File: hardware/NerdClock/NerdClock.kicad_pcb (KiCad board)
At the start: 2 copper layers, 95 x 95 mm, 0 parts

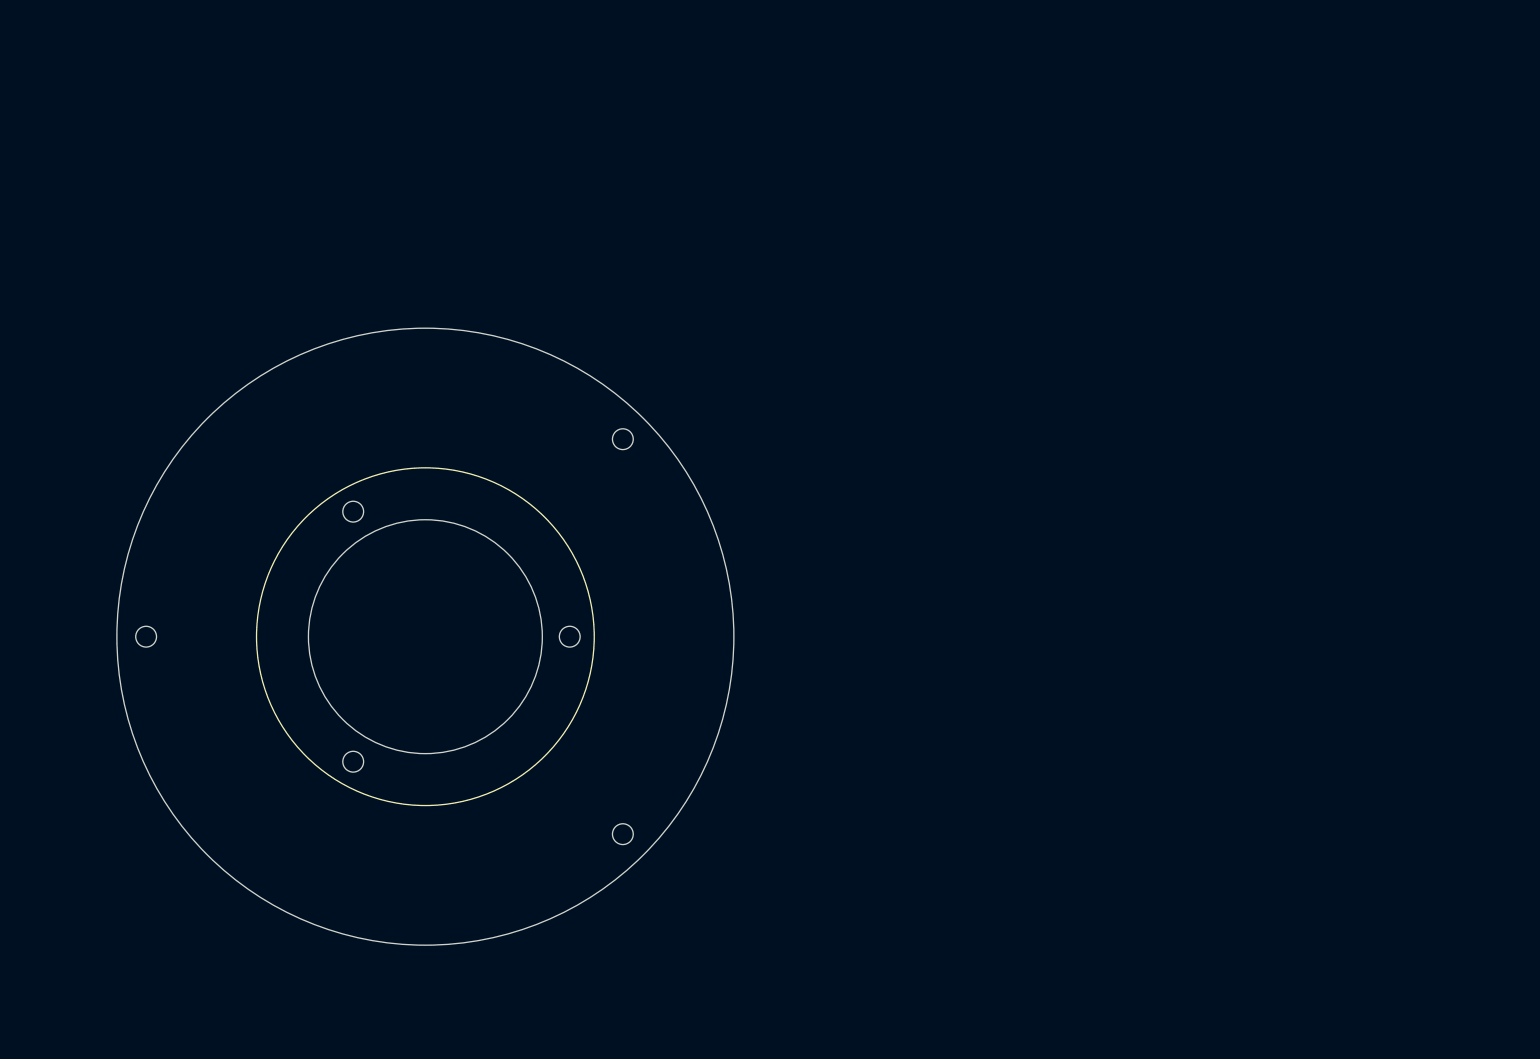
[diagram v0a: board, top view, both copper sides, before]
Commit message: Added breakout tabs
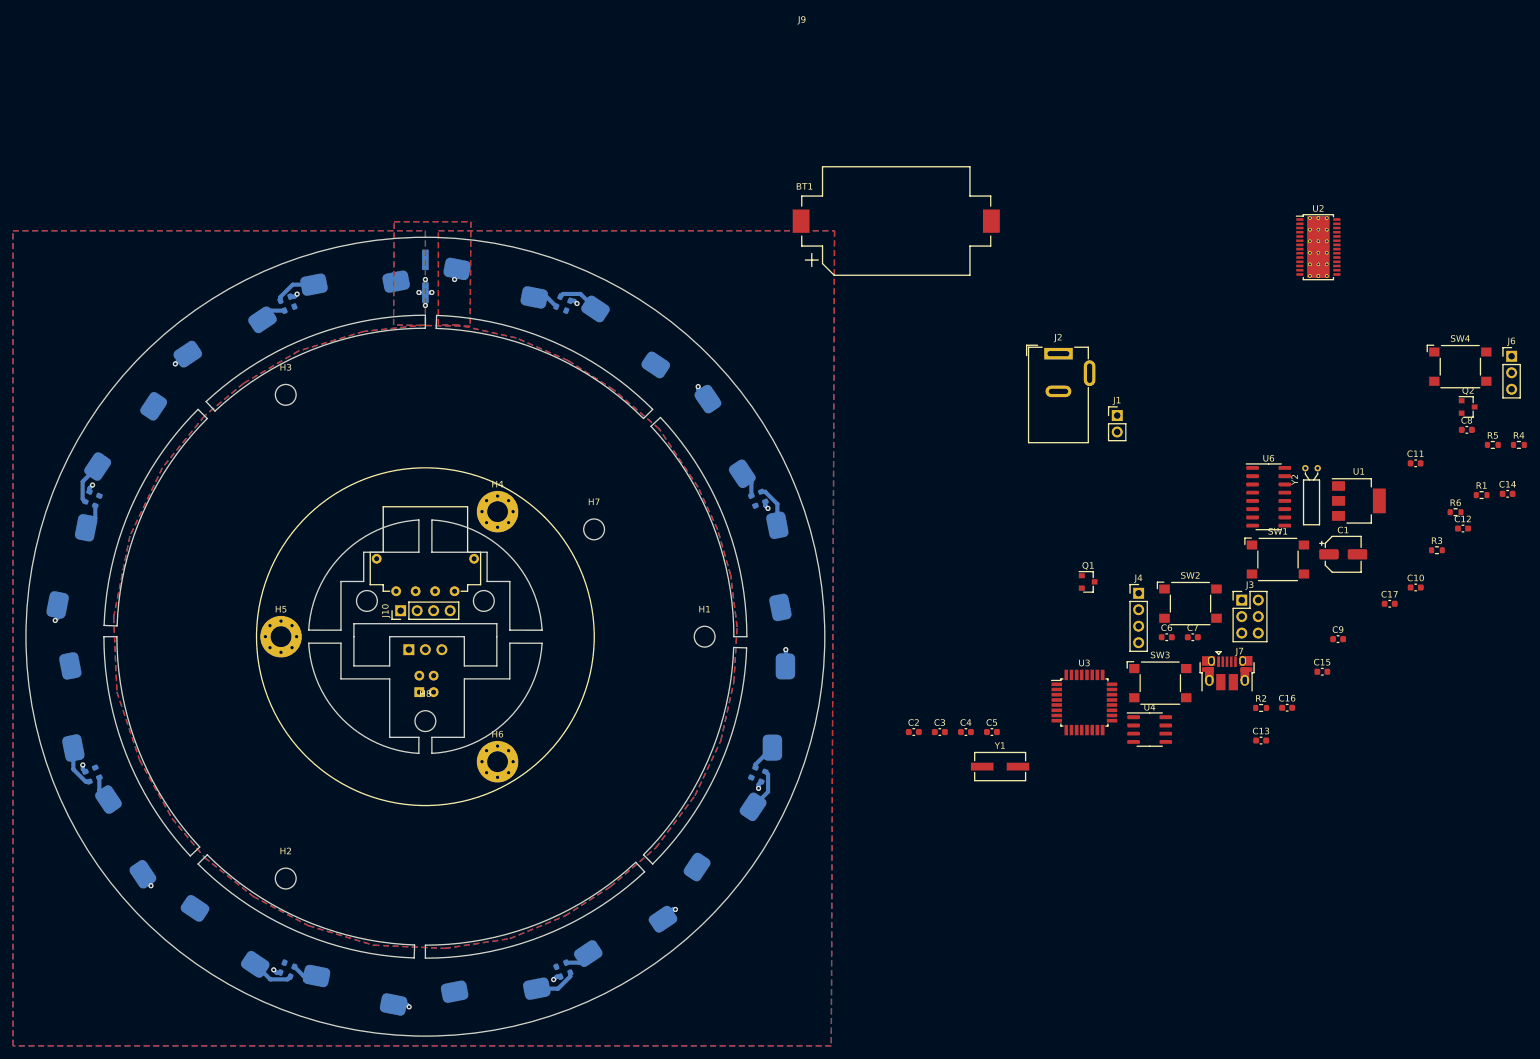
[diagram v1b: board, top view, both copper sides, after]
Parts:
- added BT1: Battery_Cell, Battery:BatteryHolder_Keystone_1060_1x2032, F.Cu at (172.5, 36.0)
- added C1: 100u, Capacitor_SMD:CP_Elec_5x5.4, F.Cu at (241.3, 87.3)
- added C10: 100n, Capacitor_SMD:C_0603_1608Metric, F.Cu at (252.5, 92.4)
- added C11: 100n, Capacitor_SMD:C_0603_1608Metric, F.Cu at (252.5, 73.3)
- added C12: 18p, Capacitor_SMD:C_0603_1608Metric, F.Cu at (259.8, 83.3)
- added C13: 0.47u, Capacitor_SMD:C_0603_1608Metric, F.Cu at (228.7, 116.0)
- added C14: 18p, Capacitor_SMD:C_0603_1608Metric, F.Cu at (266.6, 78.0)
- added C15: 100n, Capacitor_SMD:C_0603_1608Metric, F.Cu at (238.1, 105.4)
- added C16: 100n, Capacitor_SMD:C_0603_1608Metric, F.Cu at (232.7, 110.9)
- added C17: 100n, Capacitor_SMD:C_0603_1608Metric, F.Cu at (248.5, 94.9)
- added C2: 100n, Capacitor_SMD:C_0603_1608Metric, F.Cu at (175.2, 114.7)
- added C3: 10u, Capacitor_SMD:C_0603_1608Metric, F.Cu at (179.2, 114.7)
- added C4: 10n, Capacitor_SMD:C_0603_1608Metric, F.Cu at (183.2, 114.7)
- added C5: 100n, Capacitor_SMD:C_0603_1608Metric, F.Cu at (187.2, 114.7)
- added C6: 100n, Capacitor_SMD:C_0603_1608Metric, F.Cu at (214.2, 100.1)
- added C7: 100n, Capacitor_SMD:C_0603_1608Metric, F.Cu at (218.2, 100.1)
- added C8: 100n, Capacitor_SMD:C_0603_1608Metric, F.Cu at (260.4, 68.2)
- added C9: 100n, Capacitor_SMD:C_0603_1608Metric, F.Cu at (240.5, 100.4)
- added D1: LED, WhiteLed1W:WhiteLed1W, B.Cu at (110.8, 45.6)
- added D10: LED, WhiteLed1W:WhiteLed1W, B.Cu at (69.2, 146.1)
- added D11: LED, WhiteLed1W:WhiteLed1W, B.Cu at (53.9, 130.8)
- added D12: LED, WhiteLed1W:WhiteLed1W, B.Cu at (45.6, 110.8)
- added D13: LED, WhiteLed1W:WhiteLed1W, B.Cu at (45.6, 89.2)
- added D14: LED, WhiteLed1W:WhiteLed1W, B.Cu at (53.9, 69.2)
- added D15: LED, WhiteLed1W:WhiteLed1W, B.Cu at (69.2, 53.9)
- added D16: LED, WhiteLed1W:WhiteLed1W, B.Cu at (89.2, 45.6)
- added D2: LED, WhiteLed1W:WhiteLed1W, B.Cu at (130.8, 53.9)
- added D3: LED, WhiteLed1W:WhiteLed1W, B.Cu at (146.1, 69.2)
- added D4: LED, WhiteLed1W:WhiteLed1W, B.Cu at (154.4, 89.2)
- added D5: LED, WhiteLed1W:WhiteLed1W, B.Cu at (154.4, 110.8)
- added D6: LED, WhiteLed1W:WhiteLed1W, B.Cu at (146.1, 130.8)
- added D7: LED, WhiteLed1W:WhiteLed1W, B.Cu at (130.8, 146.1)
- added D8: LED, WhiteLed1W:WhiteLed1W, B.Cu at (110.8, 154.4)
- added D9: LED, WhiteLed1W:WhiteLed1W, B.Cu at (89.2, 154.4)
- added H1: MountingHole, MountingHole:MountingHole_3.2mm_M3, F.Cu at (143.0, 100.0)
- added H10: MountingHole, MountingHole:MountingHole_3.2mm_M3, F.Cu at (109.0, 94.5)
- added H2: MountingHole, MountingHole:MountingHole_3.2mm_M3, F.Cu at (78.5, 137.2)
- added H3: MountingHole, MountingHole:MountingHole_3.2mm_M3, F.Cu at (78.5, 62.8)
- added H4: MountingHole_Pad, MountingHole:MountingHole_3.2mm_M3_Pad_Via, F.Cu at (111.1, 80.7)
- added H5: MountingHole_Pad, MountingHole:MountingHole_3.2mm_M3_Pad_Via, F.Cu at (77.8, 100.0)
- added H6: MountingHole_Pad, MountingHole:MountingHole_3.2mm_M3_Pad_Via, F.Cu at (111.1, 119.3)
- added H7: MountingHole, MountingHole:MountingHole_3.2mm_M3, F.Cu at (126.0, 83.5)
- added H8: MountingHole, MountingHole:MountingHole_3.2mm_M3, F.Cu at (100.0, 113.0)
- added H9: MountingHole, MountingHole:MountingHole_3.2mm_M3, F.Cu at (91.0, 94.5)
- added J1: Conn_01x02, Connector_PinHeader_2.54mm:PinHeader_1x02_P2.54mm_Vertical, F.Cu at (206.5, 65.9)
- added J10: Conn_01x04, Connector_PinHeader_2.54mm:PinHeader_1x04_P2.54mm_Vertical, F.Cu at (96.2, 96.0)
- added J2: Jack-DC, Connector_BarrelJack:BarrelJack_Wuerth_6941xx301002, F.Cu at (197.5, 56.4)
- added J3: ICSP, Connector_PinHeader_2.54mm:PinHeader_2x03_P2.54mm_Vertical, F.Cu at (225.7, 94.4)
- added J4: Conn_01x04, Connector_PinHeader_2.54mm:PinHeader_1x04_P2.54mm_Vertical, F.Cu at (209.8, 93.3)
- added J5: Conn_01x03, Connector_PinHeader_2.54mm:PinHeader_1x03_P2.54mm_Vertical, B.Cu at (97.5, 102.0)
- added J6: Conn_01x03, Connector_PinHeader_2.54mm:PinHeader_1x03_P2.54mm_Vertical, F.Cu at (267.3, 56.8)
- added J7: USB_B_Micro, Connector_USB:USB_Micro-B_Amphenol_10103594-0001LF_Horizontal, F.Cu at (223.5, 105.6)
- added J8: Conn_01x02, Connector_PinHeader_2.54mm:PinHeader_2x01_P2.54mm_Vertical_SMD, B.Cu at (100.0, 44.5)
- added J9: Conn_01x05, MotorConn:MotorConn, F.Cu at (100.0, 93.0)
- added Q1: RTR025N03FRATL, Package_TO_SOT_SMD:SOT-23, F.Cu at (202.1, 91.6)
- added Q2: RTR025N03FRATL, Package_TO_SOT_SMD:SOT-23, F.Cu at (260.6, 64.6)
- added R1: 300R, Resistor_SMD:R_0603_1608Metric, F.Cu at (262.6, 78.2)
- added R10: 22R, Resistor_SMD:R_0603_1608Metric, B.Cu at (152.0, 78.4)
- added R11: 22R, Resistor_SMD:R_0603_1608Metric, B.Cu at (150.5, 120.9)
- added R12: 22R, Resistor_SMD:R_0603_1608Metric, B.Cu at (152.0, 121.6)
- added R13: 22R, Resistor_SMD:R_0603_1608Metric, B.Cu at (120.9, 150.5)
- added R14: 22R, Resistor_SMD:R_0603_1608Metric, B.Cu at (121.6, 152.0)
- added R15: 22R, Resistor_SMD:R_0603_1608Metric, B.Cu at (79.1, 150.5)
- added R16: 22R, Resistor_SMD:R_0603_1608Metric, B.Cu at (78.4, 152.0)
- added R17: 22R, Resistor_SMD:R_0603_1608Metric, B.Cu at (49.5, 120.9)
- added R18: 22R, Resistor_SMD:R_0603_1608Metric, B.Cu at (48.0, 121.6)
- added R19: 22R, Resistor_SMD:R_0603_1608Metric, B.Cu at (49.5, 79.1)
- added R2: 300R, Resistor_SMD:R_0603_1608Metric, F.Cu at (228.7, 111.0)
- added R20: 22R, Resistor_SMD:R_0603_1608Metric, B.Cu at (48.0, 78.4)
- added R21: 22R, Resistor_SMD:R_0603_1608Metric, B.Cu at (79.1, 49.5)
- added R22: 22R, Resistor_SMD:R_0603_1608Metric, B.Cu at (78.4, 48.0)
- added R3: 20k, Resistor_SMD:R_0603_1608Metric, F.Cu at (255.8, 86.7)
- added R4: 10k, Resistor_SMD:R_0603_1608Metric, F.Cu at (268.4, 70.5)
- added R5: 4k7, Resistor_SMD:R_0603_1608Metric, F.Cu at (264.4, 70.5)
- added R6: 4k7, Resistor_SMD:R_0603_1608Metric, F.Cu at (258.6, 80.8)
- added R7: 22R, Resistor_SMD:R_0603_1608Metric, B.Cu at (120.9, 49.5)
- added R8: 22R, Resistor_SMD:R_0603_1608Metric, B.Cu at (121.6, 48.0)
- added R9: 22R, Resistor_SMD:R_0603_1608Metric, B.Cu at (150.5, 79.1)
- added SW1: SW_MEC_5G, Button_Switch_SMD:SW_SPST_Omron_B3FS-100xP, F.Cu at (231.3, 88.1)
- added SW2: SW_MEC_5G, Button_Switch_SMD:SW_SPST_Omron_B3FS-100xP, F.Cu at (217.8, 94.9)
- added SW3: SW_MEC_5G, Button_Switch_SMD:SW_SPST_Omron_B3FS-100xP, F.Cu at (213.2, 107.2)
- added SW4: SW_MEC_5G, Button_Switch_SMD:SW_SPST_Omron_B3FS-100xP, F.Cu at (259.4, 58.4)
- added U1: IFX1117, Package_TO_SOT_SMD:SOT-223-3_TabPin2, F.Cu at (243.7, 79.1)
- added U2: DRV8313, Package_SO:HTSSOP-28-1EP_4.4x9.7mm_P0.65mm_EP3.4x9.5mm_ThermalVias, F.Cu at (237.5, 40.0)
- added U3: ATmega168P-20AU, Package_QFP:TQFP-32_7x7mm_P0.8mm, F.Cu at (201.5, 110.1)
- added U4: DS1338Z-18+, Package_SO:SOIC-8_3.9x4.9mm_P1.27mm, F.Cu at (211.5, 114.3)
- added U5: OPB706A, OPB706A:OPB706A, B.Cu at (100.2, 107.3)
- added U6: CH340C, Package_SO:SOIC-16_3.9x9.9mm_P1.27mm, F.Cu at (229.8, 78.5)
- added Y1: 16MHz, Crystal:Crystal_SMD_ECS_CSM3X-2Pin_7.6x4.1mm, F.Cu at (188.5, 120.0)
- added Y2: 32.768kHz/12.5pf, Crystal:Crystal_C26-LF_D2.1mm_L6.5mm_Horizontal, F.Cu at (235.5, 74.1)
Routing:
- net Net-(D1-Pad1): track 0.00 -> 35.1 mm, vias 0 -> 20
- net Net-(D16-Pad1): track 0.00 -> 6.54 mm
- net Net-(D12-Pad1): track 0.00 -> 6.54 mm
- net Net-(D8-Pad1): track 0.00 -> 6.54 mm
- net Net-(D4-Pad1): track 0.00 -> 6.54 mm
- net Net-(D2-Pad1): track 0.00 -> 6.54 mm
- net Net-(D14-Pad1): track 0.00 -> 6.54 mm
- net Net-(D6-Pad1): track 0.00 -> 6.54 mm
- net Net-(D10-Pad1): track 0.00 -> 6.54 mm
- net Net-(D5-Pad2): track 0.00 -> 4.16 mm
- net Net-(D15-Pad2): track 0.00 -> 3.98 mm
- net Net-(D11-Pad2): track 0.00 -> 3.98 mm
- net Net-(D7-Pad2): track 0.00 -> 3.98 mm
- net Net-(D3-Pad2): track 0.00 -> 3.98 mm
- net Net-(D9-Pad2): track 0.00 -> 3.98 mm
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- added copper zone on F.Cu, net Net-(D1-Pad1)
- added copper zone on B.Cu, net Net-(D10-Pad2)
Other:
- board size 95 x 95 mm -> 123 x 123 mm

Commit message: Put LEDs on the right side (wtffff)
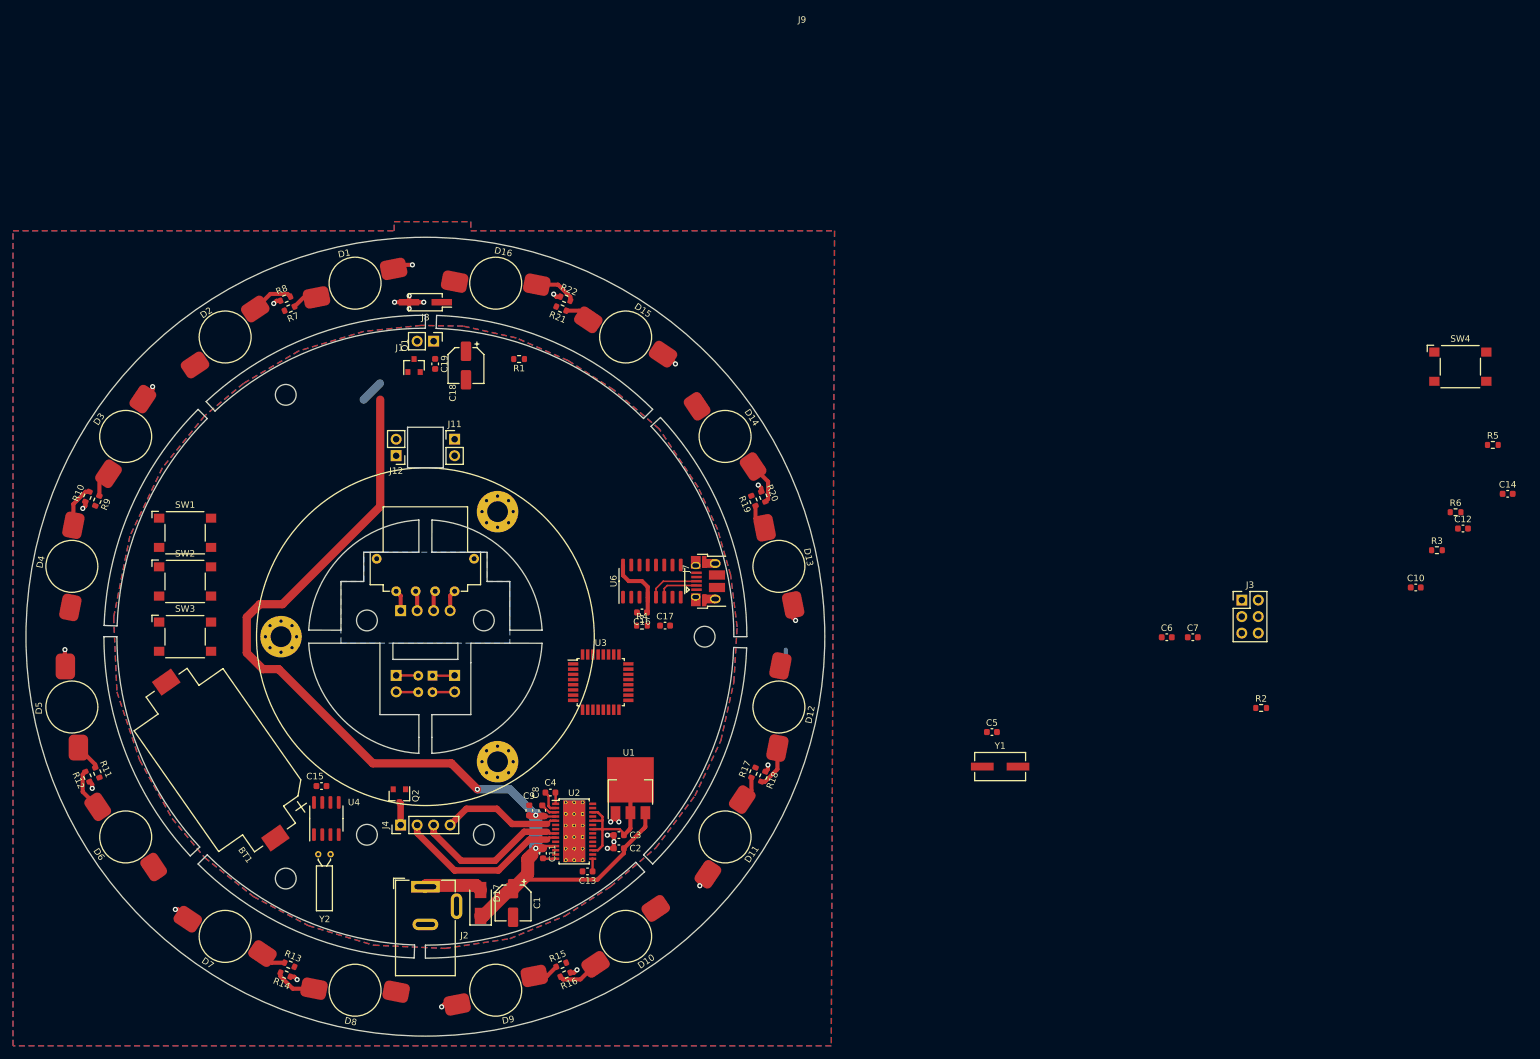
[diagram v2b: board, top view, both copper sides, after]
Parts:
- removed H7, H8: MountingHole, MountingHole:MountingHole_3.2mm_M3
- added C18: 100u, Capacitor_SMD:CP_Elec_5x5.4, F.Cu at (106.2, 58.2)
- added C19: 100n, Capacitor_SMD:C_0603_1608Metric, F.Cu at (101.5, 58.0)
- added D17: S1JL R3, Diode_SMD:D_SMA, F.Cu at (108.5, 141.0)
- added H11: MountingHole, MountingHole:MountingHole_3.2mm_M3, F.Cu at (109.0, 130.5)
- added H12: MountingHole, MountingHole:MountingHole_3.2mm_M3, F.Cu at (91.0, 130.5)
- added J11: Conn_01x02, Connector_PinHeader_2.54mm:PinHeader_1x02_P2.54mm_Vertical, F.Cu at (104.5, 69.6)
- added J12: Conn_01x02, Connector_PinHeader_2.54mm:PinHeader_1x02_P2.54mm_Vertical, F.Cu at (95.5, 72.1)
- D1, D10, D11, D12, D13, D14, D15, D16, D2, D3, D4, D5, D6, D7, D8, D9, J8, R10, R11, R12, R13, R14, R15, R16, R17, R18, R19, R20, R21, R22, R7, R8, R9: moved to F.Cu
- J10: moved to B.Cu
- J5: value Conn_01x03 -> Conn_01x02; footprint Connector_PinHeader_2.54mm:PinHeader_1x03_P2.54mm_Vertical -> Connector_PinHeader_2.54mm:PinHeader_1x02_P2.54mm_Vertical
- J6: value Conn_01x03 -> Conn_01x02; footprint Connector_PinHeader_2.54mm:PinHeader_1x03_P2.54mm_Vertical -> Connector_PinHeader_2.54mm:PinHeader_1x02_P2.54mm_Vertical; moved to B.Cu
- moved J6 178.6 mm to (95.5, 106.0), turned to 180 degrees
- moved Q2 175.1 mm to (96.0, 124.5), turned to 270 degrees
- moved SW1 168.3 mm to (63.0, 84.0)
- moved Y2 163.2 mm to (83.5, 133.5)
- moved C15 155.1 mm to (84.0, 123.0)
- moved SW2 154.8 mm to (63.0, 91.5)
- moved C8 153.9 mm to (118.0, 126.8), turned to 270 degrees
- moved SW3 150.3 mm to (63.0, 100.0)
- moved R1 149.7 mm to (114.4, 57.2), turned to 180 degrees
- moved C11 147.2 mm to (118.1, 133.3), turned to 270 degrees
- moved U2 145.7 mm to (122.9, 130.0)
- moved C1 138.6 mm to (113.5, 141.0), turned to 270 degrees
- moved R4 137.9 mm to (133.3, 98.3)
- moved BT1 133.1 mm to (68.5, 119.0), turned to 125 degrees
- moved U4 127.5 mm to (84.8, 128.0), turned to 90 degrees
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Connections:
- D10 pad 2: Net-(D10-Pad2) -> VCC
- D12 pad 2: Net-(D10-Pad2) -> VCC
- D14 pad 2: Net-(D10-Pad2) -> VCC
- D16 pad 2: Net-(D10-Pad2) -> VCC
- D2 pad 2: Net-(D10-Pad2) -> VCC
- D4 pad 2: Net-(D10-Pad2) -> VCC
- D6 pad 2: Net-(D10-Pad2) -> VCC
- D8 pad 2: Net-(D10-Pad2) -> VCC
- J1 pad 2: Net-(J1-Pad2) -> Net-(D1-Pad1)
- J2 pad 1: VCC -> Net-(D17-Pad2)
- J6 pad 1: DOT -> Net-(J6-Pad1)
- J6 pad 2: GND -> Net-(J6-Pad2)
- J8 pad 1: Net-(D10-Pad2) -> VCC
- Q1 pad 3: Net-(J1-Pad2) -> Net-(D1-Pad1)
- R11 pad 2: Net-(D10-Pad2) -> VCC
- R13 pad 2: Net-(D10-Pad2) -> VCC
- R15 pad 2: Net-(D10-Pad2) -> VCC
- R17 pad 2: Net-(D10-Pad2) -> VCC
- R19 pad 2: Net-(D10-Pad2) -> VCC
- R2 pad 1: Net-(J6-Pad3) -> Net-(J12-Pad2)
- R21 pad 2: Net-(D10-Pad2) -> VCC
- R7 pad 2: Net-(D10-Pad2) -> VCC
- R9 pad 2: Net-(D10-Pad2) -> VCC
- SW1 pad 3: Net-(SW1-Pad3) -> GND
- SW1 pad 4: Net-(SW1-Pad3) -> GND
- SW2 pad 3: Net-(SW1-Pad3) -> GND
- SW2 pad 4: Net-(SW1-Pad3) -> GND
- SW3 pad 3: Net-(SW1-Pad3) -> GND
- SW3 pad 4: Net-(SW1-Pad3) -> GND
- SW4 pad 3: Net-(SW1-Pad3) -> GND
- SW4 pad 4: Net-(SW1-Pad3) -> GND
- U5 pad 3: Net-(J5-Pad3) -> Net-(J6-Pad2)
- U5 pad 4: Net-(J5-Pad2) -> Net-(J6-Pad1)
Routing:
- net VCC: track 0.00 -> 158.8 mm, vias 0 -> 3
- net +3V3: track 0.00 -> 35.2 mm
- net Net-(J4-Pad2): track 0.00 -> 27.0 mm
- net Net-(J4-Pad3): track 0.00 -> 23.8 mm
- net Net-(J4-Pad4): track 0.00 -> 18.5 mm
- net GND: track 0.00 -> 9.38 mm, vias 0 -> 5
- net Net-(D17-Pad2): track 0.00 -> 8.87 mm
- net Net-(J7-Pad3): track 0.00 -> 8.03 mm
- net Net-(J7-Pad2): track 0.00 -> 6.49 mm
- net Net-(D1-Pad1): track 35.1 -> 39.1 mm
- net Net-(J4-Pad1): track 0.00 -> 3.58 mm
- net Net-(C4-Pad2): track 0.00 -> 3.51 mm
- net Net-(J6-Pad1): track 0.00 -> 3.47 mm
- net Net-(J6-Pad2): track 0.00 -> 3.42 mm
- net Net-(J5-Pad2): track 0.00 -> 3.42 mm
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- added copper zone on B.Cu, net Net-(D1-Pad1)
- added copper zone on B.Cu, net Net-(J9-Pad5)
- added copper zone on F.Cu, net VCC
- removed copper zone on F.Cu, net Net-(D1-Pad1)
- removed copper zone on B.Cu, net Net-(D10-Pad2)
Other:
- outline, holes or cut-outs redrawn

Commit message: Routing backup
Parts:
- moved R5 184.0 mm to (87.8, 122.2), turned to 90 degrees
- moved R6 173.8 mm to (89.8, 122.2), turned to 90 degrees
- moved R3 155.6 mm to (101.5, 66.5)
- moved C14 149.9 mm to (120.9, 113.2), turned to 180 degrees
- moved C12 145.2 mm to (117.7, 113.2)
- moved R2 138.4 mm to (97.9, 65.9)
- moved SW4 137.4 mm to (125.9, 91.3), turned to 270 degrees
- moved C10 119.1 mm to (134.3, 107.0), turned to 180 degrees
- moved C7 98.7 mm to (119.8, 108.0), turned to 180 degrees
- moved J3 85.6 mm to (141.7, 110.8), turned to 180 degrees
- moved C6 80.4 mm to (134.3, 109.1)
- moved Y1 69.0 mm to (119.5, 116.3)
- moved C5 68.0 mm to (119.8, 106.0), turned to 180 degrees
- moved C17 12.7 mm to (133.2, 86.2)
- moved C18 12.5 mm to (93.8, 57.8)
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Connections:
- U3 pad 11: SW3 -> DC_BRAKE
- U3 pad 24: DC_BRAKE -> SW3
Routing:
- net +3V3: track 35.2 -> 185.8 mm, vias 0 -> 8
- net PPS: track 0.00 -> 69.5 mm, vias 0 -> 2
- net SDA: track 0.00 -> 66.9 mm, vias 0 -> 2
- net SCL: track 0.00 -> 63.5 mm, vias 0 -> 2
- net DC_BRAKE: track 0.00 -> 45.6 mm, vias 0 -> 2
- net nCPU_RESET: track 0.00 -> 38.3 mm, vias 0 -> 2
- net nMOTOR_RESET: track 0.00 -> 29.3 mm, vias 0 -> 2
- net nFAULT: track 0.00 -> 24.7 mm, vias 0 -> 2
- net LED: track 0.00 -> 24.2 mm
- net W: track 0.00 -> 20.4 mm
- net V: track 0.00 -> 18.8 mm
- net VCC: track 158.8 -> 177.0 mm
- net CPU_TX: track 0.00 -> 17.3 mm
- net U: track 0.00 -> 17.3 mm
- net Net-(J3-Pad1): track 0.00 -> 13.7 mm
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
